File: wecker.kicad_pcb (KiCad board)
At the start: 2 copper layers, 85.1 x 31.8 mm, 2 parts, among them J1 Conn_01x20, U1 MSP430FR4133

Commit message: added some more parts
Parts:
- added C1: 0.1µF, Capacitor_SMD:C_1206_3216Metric_Pad1.42x1.75mm_HandSolder, F.Cu at (96.5, 96.6)
- added C2: 0.1µF, Capacitor_SMD:C_1206_3216Metric_Pad1.42x1.75mm_HandSolder, F.Cu at (105.1, 79.4)
- added C3: 0.1µF, Capacitor_SMD:C_1206_3216Metric_Pad1.42x1.75mm_HandSolder, F.Cu at (118.1, 82.6)
- added C4: 0.1µF, Capacitor_SMD:C_1206_3216Metric_Pad1.42x1.75mm_HandSolder, F.Cu at (111.2, 93.1)
- added D1: LED_BG, LED_SMD:LED_1210_3225Metric_Pad1.42x2.65mm_HandSolder, F.Cu at (90.6, 97.1)
- added D2: LED_BG, LED_SMD:LED_1210_3225Metric_Pad1.42x2.65mm_HandSolder, F.Cu at (118.1, 78.8)
- added J2: Conn_01x05_Male, Connector_PinHeader_2.54mm:PinHeader_1x05_P2.54mm_Horizontal, F.Cu at (93.2, 79.2)
- added Q1: PN2222A, Package_TO_SOT_THT:TO-92_Inline, F.Cu at (103.7, 94.7)
- added R1: R, Resistor_SMD:R_1210_3225Metric_Pad1.42x2.65mm_HandSolder, F.Cu at (118.1, 86.3)
- added SW1: Hour, Button_Switch_SMD:SW_SPST_B3U-1000P, F.Cu at (124.0, 82.1)
- added SW2: Minute, Button_Switch_SMD:SW_SPST_B3U-1000P, F.Cu at (118.0, 90.6)
- added SW3: Snooze, Button_Switch_SMD:SW_SPST_B3U-1000P, F.Cu at (111.1, 96.9)
- added TP1: ClockInput, Connector_Wire:SolderWirePad_1x01_Drill1.2mm, F.Cu at (123.8, 87.0)
- added Y1: 32.768 kHz, Crystal:Crystal_HC18-U_Horizontal, F.Cu at (77.8, 69.1)
- J1: moved to B.Cu
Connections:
- U1 pad 10: (no net) -> Net-(C1-Pad2)
- U1 pad 11: (no net) -> Net-(C1-Pad1)
- U1 pad 12: (no net) -> Net-(U1-Pad12)
- U1 pad 13: (no net) -> Net-(U1-Pad13)
- U1 pad 14: (no net) -> GND
- U1 pad 15: (no net) -> +BATT
- U1 pad 16: (no net) -> Net-(J2-Pad3)
- U1 pad 17: (no net) -> Net-(J2-Pad2)
- U1 pad 18: (no net) -> GND
- U1 pad 19: (no net) -> GND
- U1 pad 20: (no net) -> Net-(TP1-Pad1)
- U1 pad 21: (no net) -> GND
- U1 pad 22: (no net) -> GND
- U1 pad 23: (no net) -> GND
- U1 pad 24: (no net) -> GND
- U1 pad 25: (no net) -> Net-(J2-Pad5)
- U1 pad 26: (no net) -> Net-(J2-Pad4)
- U1 pad 27: (no net) -> Net-(J1-Pad20)
- U1 pad 28: (no net) -> Net-(J1-Pad19)
- U1 pad 29: (no net) -> Net-(J1-Pad18)
- U1 pad 30: (no net) -> Net-(J1-Pad17)
- U1 pad 31: (no net) -> GND
- U1 pad 32: (no net) -> GND
- U1 pad 33: (no net) -> GND
- U1 pad 34: (no net) -> Net-(Q1-Pad2)
- U1 pad 35: Net-(J1-Pad20) -> GND
- U1 pad 36: Net-(J1-Pad19) -> Net-(SW3-Pad1)
- U1 pad 37: Net-(J1-Pad18) -> Net-(SW2-Pad1)
- U1 pad 38: Net-(J1-Pad17) -> Net-(SW1-Pad1)
- U1 pad 7: (no net) -> Net-(C4-Pad1)
- U1 pad 8: (no net) -> Net-(C3-Pad1)
- U1 pad 9: (no net) -> Net-(C2-Pad2)
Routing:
- net GND: track 0.00 -> 34.2 mm
- net Net-(J2-Pad5): track 0.00 -> 34.0 mm
- net Net-(J2-Pad4): track 0.00 -> 31.0 mm
- net Net-(U1-Pad13): track 0.00 -> 28.3 mm
- net Net-(U1-Pad12): track 0.00 -> 27.8 mm
- net Net-(J2-Pad3): track 0.00 -> 21.5 mm
- net Net-(J1-Pad1): track 39.5 -> 19.9 mm, vias 0 -> 1
- net Net-(J2-Pad2): track 0.00 -> 18.7 mm
- net Net-(J1-Pad2): track 35.8 -> 17.9 mm, vias 0 -> 1
- net Net-(J1-Pad3): track 32.2 -> 15.7 mm, vias 0 -> 1
- net Net-(J1-Pad4): track 28.5 -> 13.7 mm, vias 0 -> 1
- net Net-(J1-Pad5): track 24.9 -> 11.7 mm, vias 0 -> 1
- net Net-(J1-Pad6): track 21.2 -> 9.38 mm, vias 0 -> 1
- net Net-(J1-Pad7): track 25.0 -> 15.0 mm, vias 0 -> 1
- net Net-(J1-Pad8): track 23.8 -> 13.8 mm, vias 0 -> 1
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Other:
- board size 85.1 x 31.8 mm -> 85.1 x 50.8 mm

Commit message: exchange some parts
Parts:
- J2: footprint Connector_PinHeader_2.54mm:PinHeader_1x05_P2.54mm_Horizontal -> Connector_PinHeader_2.54mm:PinHeader_1x05_P2.54mm_Vertical
- Q1: value PN2222A -> BC818; footprint Package_TO_SOT_THT:TO-92_Inline -> Package_TO_SOT_SMD:SOT-23
- Y1: footprint Crystal:Crystal_HC18-U_Horizontal -> Crystal:Crystal_DS26_D2.0mm_L6.0mm_Horizontal
- moved D1 49.1 mm to (134.4, 74.9)
- moved SW3 36.8 mm to (128.3, 64.3), turned to 270 degrees
- moved C4 34.4 mm to (90.2, 65.8), turned to 270 degrees
- moved C1 30.8 mm to (97.8, 65.8), turned to 90 degrees
- moved C3 30.4 mm to (92.7, 65.8), turned to 270 degrees
- moved Q1 27.8 mm to (124.5, 76.2)
- moved TP1 27.6 mm to (99.7, 73.7)
- moved SW2 26.8 mm to (123.2, 64.3), turned to 270 degrees
- moved Y1 25.1 mm to (102.9, 67.9), turned to 180 degrees
- moved SW1 18.7 mm to (118.1, 64.3), turned to 270 degrees
- moved D2 18.6 mm to (134.4, 69.8)
- moved C2 16.8 mm to (95.2, 65.8), turned to 90 degrees
- moved R1 16.2 mm to (123.2, 70.9), turned to 270 degrees
- moved J2 13.2 mm to (106.0, 76.2), turned to 90 degrees
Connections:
- Q1 pad 1: GND -> Net-(Q1-Pad1)
- Q1 pad 2: Net-(Q1-Pad2) -> GND
- U1 pad 34: Net-(Q1-Pad2) -> Net-(Q1-Pad1)
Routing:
- net +BATT: track 0.00 -> 27.8 mm, vias 0 -> 2
- net Net-(J2-Pad5): track 34.0 -> 6.20 mm
- net Net-(U1-Pad13): track 28.3 -> 3.12 mm
- net Net-(J2-Pad4): track 31.0 -> 6.56 mm
- net Net-(U1-Pad12): track 27.8 -> 4.81 mm
- net Net-(D1-Pad2): track 0.00 -> 20.2 mm
- net Net-(SW3-Pad1): track 0.00 -> 17.4 mm
- net Net-(C4-Pad1): track 0.00 -> 15.9 mm
- net Net-(Q1-Pad1): track 0.00 -> 14.4 mm
- net GND: track 34.2 -> 47.7 mm, vias 0 -> 4
- net Net-(C3-Pad1): track 0.00 -> 13.2 mm
- net Net-(D1-Pad1): track 0.00 -> 13.1 mm
- net Net-(SW2-Pad1): track 0.00 -> 12.1 mm
- net Net-(C2-Pad2): track 0.00 -> 10.5 mm
- net Net-(J2-Pad3): track 21.5 -> 12.6 mm
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- added copper zone on B.Cu, net GND
- added copper zone on F.Cu, net GND
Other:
- outline, holes or cut-outs redrawn

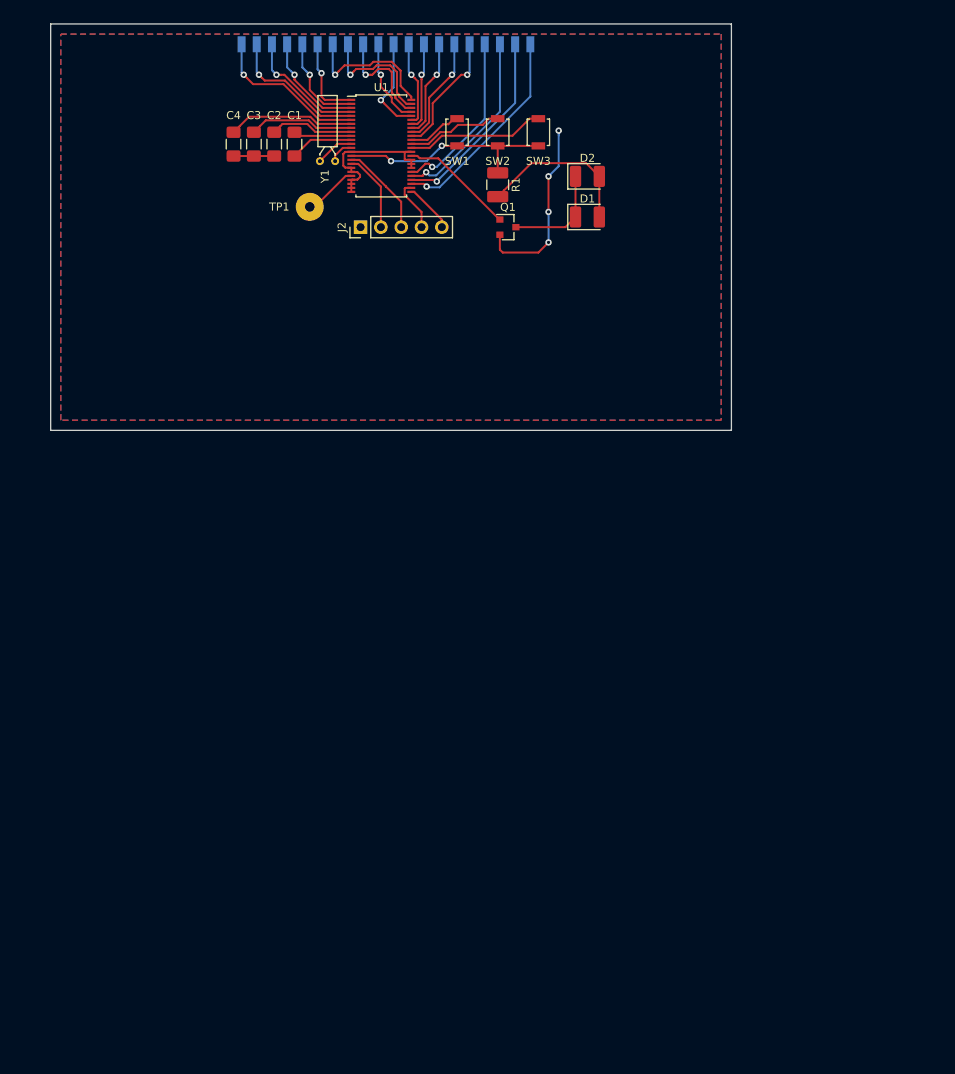
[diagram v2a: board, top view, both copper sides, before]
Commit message: correct PCB Measurements
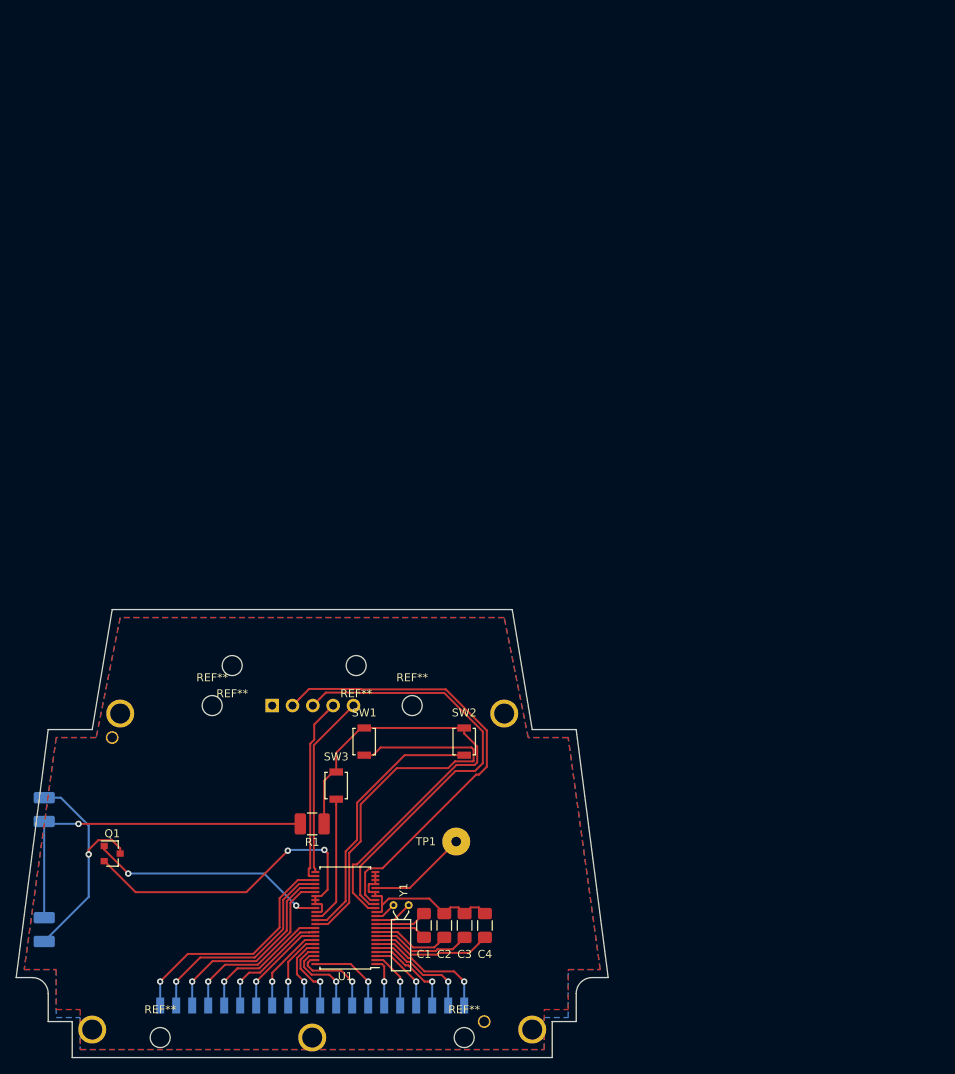
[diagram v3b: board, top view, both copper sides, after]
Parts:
- added REF**: MountingHole_2.5mm, MountingHole:MountingHole_2.5mm, F.Cu at (105.5, 131.0)
- added REF**: MountingHole_2.5mm, MountingHole:MountingHole_2.5mm, F.Cu at (90.0, 131.0)
- added REF**: MountingHole_2.5mm, MountingHole:MountingHole_2.5mm, F.Cu at (87.5, 136.0)
- added REF**: MountingHole_2.5mm, MountingHole:MountingHole_2.5mm, F.Cu at (112.5, 136.0)
- added REF**: MountingHole_2.5mm, MountingHole:MountingHole_2.5mm, F.Cu at (81.0, 177.5)
- added REF**: MountingHole_2.5mm, MountingHole:MountingHole_2.5mm, F.Cu at (119.0, 177.5)
- D1, D2, J2: moved to B.Cu
- moved J1 122.0 mm to (100.0, 175.0), turned to 180 degrees
- moved D1 112.0 mm to (66.5, 164.0), turned to 90 degrees
- moved D2 104.3 mm to (66.5, 149.0), turned to 270 degrees
- moved C4 102.6 mm to (121.6, 163.5), turned to 90 degrees
- moved C3 101.2 mm to (119.0, 163.5), turned to 90 degrees
- moved C2 100.0 mm to (116.5, 163.5), turned to 270 degrees
- moved C1 99.0 mm to (114.0, 163.5), turned to 270 degrees
- moved U1 96.6 mm to (104.1, 162.6), turned to 180 degrees
- moved Y1 93.3 mm to (110.2, 160.9), turned to 0 degrees
- moved Q1 92.6 mm to (75.0, 154.5)
- moved SW3 85.5 mm to (103.0, 146.0), turned to 90 degrees
- moved R1 83.2 mm to (100.0, 150.8), turned to 180 degrees
- moved TP1 81.4 mm to (118.0, 153.0)
- moved SW1 77.0 mm to (106.5, 140.5), turned to 90 degrees
- moved SW2 76.3 mm to (119.0, 140.5), turned to 90 degrees
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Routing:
- net Net-(J2-Pad2): track 9.95 -> 56.9 mm
- net Net-(SW1-Pad1): track 6.82 -> 50.2 mm
- net Net-(J2-Pad3): track 12.6 -> 54.5 mm
- net +BATT: track 27.8 -> 60.0 mm, vias 2 -> 0
- net Net-(D1-Pad2): track 20.2 -> 44.2 mm, vias 0 -> 1
- net Net-(SW2-Pad1): track 12.1 -> 33.5 mm
- net GND: track 47.7 -> 65.3 mm, vias 4 -> 2
- net Net-(J2-Pad4): track 6.56 -> 23.5 mm
- net Net-(D1-Pad1): track 13.1 -> 29.9 mm, vias 0 -> 1
- net Net-(J2-Pad5): track 6.20 -> 22.9 mm
- net Net-(Q1-Pad1): track 14.4 -> 29.9 mm, vias 0 -> 2
- net Net-(J1-Pad7): track 17.5 -> 10.5 mm
- net Net-(TP1-Pad1): track 6.80 -> 12.5 mm
- net Net-(J1-Pad8): track 15.7 -> 10.8 mm
- net Net-(J1-Pad6): track 10.6 -> 6.14 mm
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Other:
- board size 85.1 x 50.8 mm -> 74 x 56 mm

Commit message: still not ready
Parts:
- removed TP1: ClockInput, Connector_Wire:SolderWirePad_1x01_Drill1.2mm
- added BZ1: Buzzer, Buzzer_Beeper:Buzzer_12x9.5RM7.6, F.Cu at (144.2, 172.9)
- added C5: 1nF, Capacitor_SMD:C_1206_3216Metric_Pad1.42x1.75mm_HandSolder, F.Cu at (144.9, 155.7)
- added C6: 10u/10V, Capacitor_SMD:C_0603_1608Metric_Pad1.05x0.95mm_HandSolder, F.Cu at (156.9, 167.4)
- added C7: 100n, Capacitor_SMD:C_1206_3216Metric_Pad1.42x1.75mm_HandSolder, F.Cu at (150.8, 155.7)
- added C8: 12p, Capacitor_SMD:C_0603_1608Metric_Pad1.05x0.95mm_HandSolder, F.Cu at (148.8, 158.6)
- added C9: 12p, Capacitor_SMD:C_0603_1608Metric_Pad1.05x0.95mm_HandSolder, F.Cu at (170.9, 155.5)
- added D3: 1N4148, Diode_SMD:D_0805_2012Metric_Pad1.15x1.40mm_HandSolder, F.Cu at (144.3, 158.9)
- added J2: Conn_01x05, Connector_PinHeader_2.54mm:PinHeader_1x05_P2.54mm_Horizontal, F.Cu at (144.2, 141.6)
- added J3: Conn_01x04, Connector_PinHeader_2.54mm:PinHeader_1x04_P2.54mm_Horizontal, F.Cu at (157.6, 141.6)
- added J4: Conn_01x02, Connector_PinHeader_2.54mm:PinHeader_1x02_P2.54mm_Horizontal, F.Cu at (157.6, 153.8)
- added Q2: BC847, Package_TO_SOT_SMD:SOT-23, F.Cu at (175.5, 145.9)
- added R2: 47K, Resistor_SMD:R_0603_1608Metric_Pad1.05x0.95mm_HandSolder, F.Cu at (176.7, 149.4)
- added R3: R, Resistor_SMD:R_0603_1608Metric_Pad1.05x0.95mm_HandSolder, F.Cu at (170.9, 158.0)
- added SW4: Time, Button_Switch_SMD:SW_SPST_B3U-1000P, F.Cu at (81.0, 140.5)
- added SW5: Snooze, Button_Switch_SMD:SW_SPST_B3U-1000P, F.Cu at (173.7, 138.1)
- C1: value 0.1µF -> 1u
- C2, C3, C4: value 0.1µF -> 100n
- SW3: value Snooze -> Alarm
- Y1: value 32.768 kHz -> 32.768; footprint Crystal:Crystal_DS26_D2.0mm_L6.0mm_Horizontal -> Crystal:Crystal_DS26_D2.0mm_L6.0mm_Horizontal_1EP_style1
- moved SW3 11.0 mm to (93.5, 140.5)
- moved Y1 4.02 mm to (114.0, 159.7), turned to 90 degrees
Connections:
- net Net-(J1-Pad1) renamed /L1
- net Net-(J1-Pad10) renamed /L10
- net Net-(J1-Pad11) renamed /L11
- net Net-(J1-Pad12) renamed /L12
- net Net-(J1-Pad13) renamed /L13
- net Net-(J1-Pad14) renamed /L14
- net Net-(J1-Pad15) renamed /L15
- net Net-(J1-Pad16) renamed /L16
- net Net-(J1-Pad17) renamed /L17
- net Net-(J1-Pad18) renamed /L18
- net Net-(J1-Pad19) renamed /L19
- net Net-(J1-Pad2) renamed /L2
- net Net-(J1-Pad20) renamed /L20
- net Net-(J1-Pad3) renamed /L3
- net Net-(J1-Pad4) renamed /L4
- net Net-(J1-Pad5) renamed /L5
- net Net-(J1-Pad6) renamed /L6
- net Net-(J1-Pad7) renamed /L7
- net Net-(J1-Pad8) renamed /L8
- net Net-(J1-Pad9) renamed /L9
- Q1 pad 1: Net-(Q1-Pad1) -> LED
- U1 pad 12: Net-(U1-Pad12) -> Net-(C9-Pad1)
- U1 pad 13: Net-(U1-Pad13) -> Net-(C8-Pad1)
- U1 pad 16: Net-(J2-Pad3) -> Net-(C5-Pad2)
- U1 pad 18: GND -> Net-(U1-Pad18)
- U1 pad 19: GND -> Buzzer
- U1 pad 20: Net-(TP1-Pad1) -> DCF77
- U1 pad 21: GND -> Net-(U1-Pad21)
- U1 pad 22: GND -> Net-(U1-Pad22)
- U1 pad 23: GND -> Net-(U1-Pad23)
- U1 pad 24: GND -> Net-(U1-Pad24)
- U1 pad 31: GND -> Net-(U1-Pad31)
- U1 pad 32: GND -> PON
- U1 pad 33: GND -> LED
- U1 pad 34: Net-(Q1-Pad1) -> Net-(SW5-Pad1)
- U1 pad 35: GND -> Net-(SW4-Pad1)
- Y1 pad 1: Net-(U1-Pad13) -> Net-(C9-Pad1)
- Y1 pad 2: Net-(U1-Pad12) -> Net-(C8-Pad1)
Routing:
- net GND: track 65.3 -> 38.3 mm
- net +BATT: track 60.0 -> 83.2 mm, vias 0 -> 2
- net Net-(SW3-Pad1): track 16.2 -> 28.8 mm, vias 0 -> 2
- net Net-(TP1-Pad1): track 12.5 -> 0.00 mm
- net Net-(C8-Pad1): track 0.00 -> 7.96 mm
- net Net-(C9-Pad1): track 0.00 -> 7.38 mm
- net Net-(U1-Pad12): track 4.94 -> 0.00 mm
- net Net-(U1-Pad13): track 2.83 -> 0.00 mm

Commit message: some more corrections
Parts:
- removed D3: 1N4148, Diode_SMD:D_0805_2012Metric_Pad1.15x1.40mm_HandSolder
- removed the J2 at (95.0, 136.0)
- removed REF** (x6): MountingHole_2.5mm, MountingHole:MountingHole_2.5mm
- added R4: 1k, Resistor_SMD:R_0805_2012Metric_Pad1.15x1.40mm_HandSolder, F.Cu at (136.1, 131.7)
- BZ1: footprint Buzzer_Beeper:Buzzer_12x9.5RM7.6 -> Buzzer_Beeper:Buzzer_TDK_PS1240P02BT_D12.2mm_H6.5mm
- C1, C2, C3, C4, C5, C7: footprint Capacitor_SMD:C_1206_3216Metric_Pad1.42x1.75mm_HandSolder -> Capacitor_SMD:C_0805_2012Metric_Pad1.15x1.40mm_HandSolder
- C6, C8, C9: footprint Capacitor_SMD:C_0603_1608Metric_Pad1.05x0.95mm_HandSolder -> Capacitor_SMD:C_0805_2012Metric_Pad1.15x1.40mm_HandSolder
- R1: value R -> 1K; footprint Resistor_SMD:R_1210_3225Metric_Pad1.42x2.65mm_HandSolder -> Resistor_SMD:R_0805_2012Metric_Pad1.15x1.40mm_HandSolder
- R2: footprint Resistor_SMD:R_0603_1608Metric_Pad1.05x0.95mm_HandSolder -> Resistor_SMD:R_0805_2012Metric_Pad1.15x1.40mm_HandSolder
- R3: value R -> 1K; footprint Resistor_SMD:R_0603_1608Metric_Pad1.05x0.95mm_HandSolder -> Resistor_SMD:R_0805_2012Metric_Pad1.15x1.40mm_HandSolder
- moved BZ1 74.4 mm to (82.2, 131.7)
- moved C9 55.7 mm to (115.2, 153.6)
- moved C8 33.7 mm to (115.2, 160.4)
- moved Y1 1.30 mm to (114.2, 158.4)
- moved C1 1.02 mm to (114.0, 164.5)
- moved C2 1.02 mm to (116.5, 164.5)
- moved C3 1.02 mm to (119.0, 164.5)
- moved C4 1.02 mm to (121.6, 164.5)
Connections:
- C8 pad 2: GND -> GNDS
- C9 pad 2: GND -> GNDS
- D1 pad 2: Net-(D1-Pad2) -> +BATT
- D2 pad 2: Net-(D1-Pad2) -> +BATT
- Q1 pad 1: LED -> Net-(Q1-Pad1)
- Q2 pad 1: Buzzer -> Net-(Q2-Pad1)
- Q2 pad 3: Net-(Q2-Pad3) -> GND
- R1 pad 1: +BATT -> LED
- R1 pad 2: Net-(D1-Pad2) -> Net-(Q1-Pad1)
- R3 pad 1: Net-(Q2-Pad3) -> Buzzer
- R3 pad 2: GND -> Net-(Q2-Pad1)
- U1 pad 12: Net-(C9-Pad1) -> Net-(C8-Pad1)
- U1 pad 13: Net-(C8-Pad1) -> Net-(C9-Pad1)
- U1 pad 18: Net-(U1-Pad18) -> (no net)
- U1 pad 21: Net-(U1-Pad21) -> (no net)
- U1 pad 22: Net-(U1-Pad22) -> (no net)
- U1 pad 23: Net-(U1-Pad23) -> (no net)
- U1 pad 24: Net-(U1-Pad24) -> (no net)
- U1 pad 31: Net-(U1-Pad31) -> (no net)
- Y1 pad 1: Net-(C9-Pad1) -> Net-(C8-Pad1)
- Y1 pad 2: Net-(C8-Pad1) -> Net-(C9-Pad1)
- Y1 pad 3: GND -> GNDS
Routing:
- net Net-(J2-Pad2): track 56.9 -> 0.00 mm
- net Net-(J2-Pad3): track 54.5 -> 0.00 mm
- net Net-(J2-Pad4): track 23.5 -> 0.00 mm
- net Net-(J2-Pad5): track 22.9 -> 0.00 mm
- net GNDS: track 0.00 -> 13.8 mm, vias 0 -> 2
- net Net-(C9-Pad1): track 7.38 -> 11.8 mm
- net Net-(C8-Pad1): track 7.96 -> 10.2 mm
- added copper zone on B.Cu, net GNDS
- added copper zone on F.Cu, net GNDS
